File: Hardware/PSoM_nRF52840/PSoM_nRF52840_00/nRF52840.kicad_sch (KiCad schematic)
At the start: 34 parts, among them J401 Conn_01x01_Pin, J402 Conn_01x01_Pin, U401 nRF52840-QIAA-aQFN73, Y401 830108161301

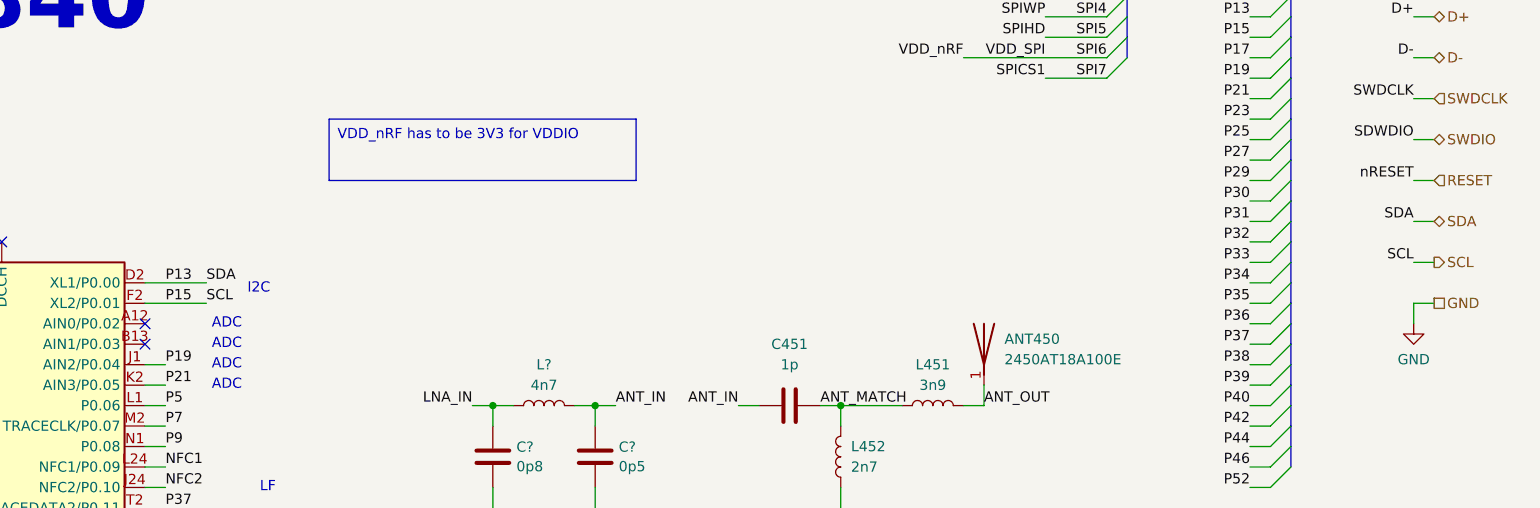
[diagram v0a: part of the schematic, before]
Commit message: moved the nrf away from the npm
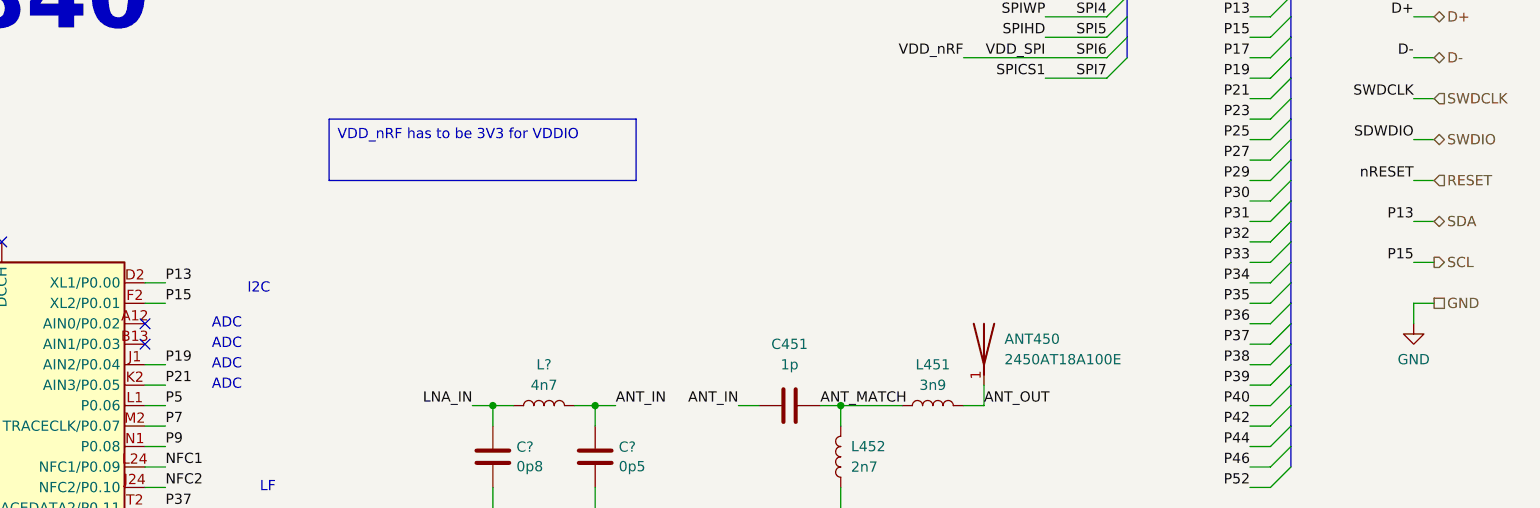
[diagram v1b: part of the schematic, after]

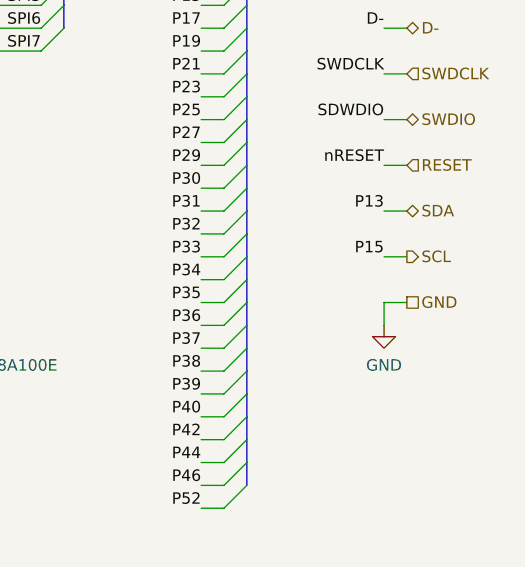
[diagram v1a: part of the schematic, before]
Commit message: moved the nrf away and re routed everything
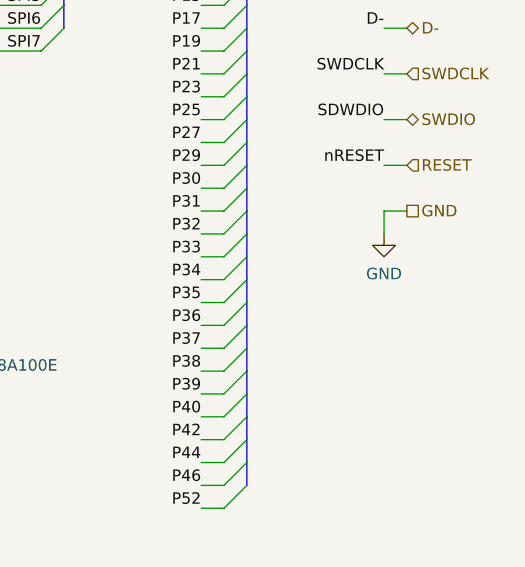
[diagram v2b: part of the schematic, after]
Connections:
- net SCL renamed P15
- net SDA renamed P13
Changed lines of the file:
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@@
 	(wire
 		(pts
-			(xy 269.24 58.42) (xy 271.78 58.42)
-		)
-		(stroke
-			(width 0)
-			(type default)
-		)
-	)
-	(wire
-		(pts
 			(xy 154.94 134.62) (xy 167.64 134.62)
 		)
@@
 	(wire
 		(pts
-			(xy 269.24 68.58) (xy 271.78 68.58)
+			(xy 269.24 58.42) (xy 271.78 58.42)
 		)
 		(stroke
@@
 	(wire
 		(pts
-			(xy 269.24 63.5) (xy 271.78 63.5)
-		)
-		(stroke
-			(width 0)
-			(type default)
-		)
-	)
-	(wire
-		(pts
 			(xy 167.64 144.78) (xy 167.64 147.32)
 		)
@@
 	(wire
 		(pts
-			(xy 269.24 71.12) (xy 269.24 68.58)
+			(xy 269.24 60.96) (xy 269.24 58.42)
 		)
 		(stroke
@@
 		)
 	)
-	(label "P15"
-		(at 269.24 63.5 180)
-		(effects
-			(font
-				(size 1.27 1.27)
-			)
-			(justify right bottom)
-		)
-	)
 	(label "SPI3"
 		(at 231.14 30.48 180)
@@
 		)
 	)
-	(label "P13"
-		(at 269.24 58.42 180)
-		(effects
-			(font
-				(size 1.27 1.27)
-			)
-			(justify right bottom)
-		)
-	)
 	(label "SPID"
 		(at 223.52 22.86 180)
@@
 		)
 	)
-	(hierarchical_label "SCL"
-		(shape output)
-		(at 271.78 63.5 0)
-		(effects
-			(font
-				(size 1.27 1.27)
-			)
-			(justify left)
-		)
-	)
-	(hierarchical_label "SDA"
-		(shape bidirectional)
-		(at 271.78 58.42 0)
-		(effects
-			(font
-				(size 1.27 1.27)
-			)
-			(justify left)
-		)
-	)
 	(hierarchical_label "RESET"
 		(shape input)
@@
 	(hierarchical_label "GND"
 		(shape passive)
-		(at 271.78 68.58 0)
+		(at 271.78 58.42 0)
 		(effects
 			(font
@@
 	(symbol
 		(lib_id "power:GND")
-		(at 269.24 71.12 0)
+		(at 269.24 60.96 0)
 		(unit 1)
 		(exclude_from_sim no)
@@
 		(fields_autoplaced yes)
 		(property "Reference" "#PWR?"
-			(at 269.24 77.47 0)
+			(at 269.24 67.31 0)
 			(effects
 				(font
@@
 		)
 		(property "Value" "GND"
-			(at 269.24 75.5634 0)
+			(at 269.24 65.4034 0)
 			(effects
 				(font
@@
 		)
 		(property "Footprint" ""
-			(at 269.24 71.12 0)
+			(at 269.24 60.96 0)
 			(effects
 				(font
@@
 		)
 		(property "Datasheet" ""
-			(at 269.24 71.12 0)
+			(at 269.24 60.96 0)
 			(effects
 				(font
@@
 		)
 		(property "Description" ""
-			(at 269.24 71.12 0)
+			(at 269.24 60.96 0)
 			(effects
 				(font

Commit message: TODO: RF and GND vias
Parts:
- removed D?: LED, LED_SMD:LED_0402_1005Metric, symbol Component lib:LED
- removed R?: 2k, Resistor_SMD:R_0402_1005Metric, symbol Component lib:R

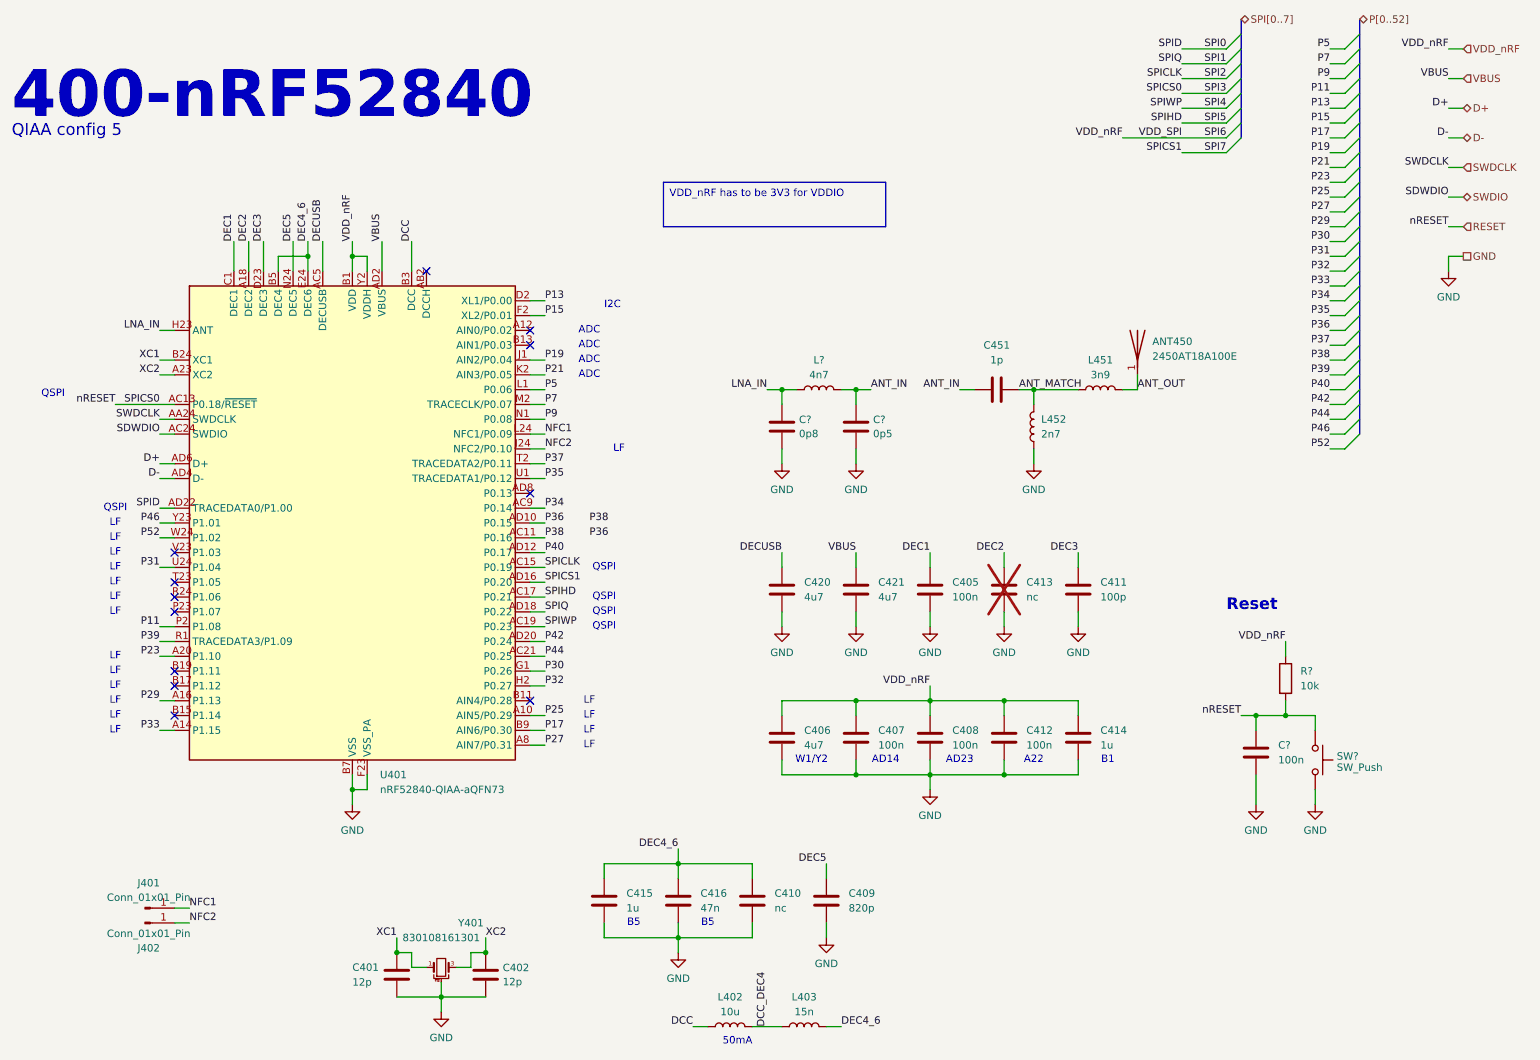
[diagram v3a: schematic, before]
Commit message: added ufl connector and trace width for 50ohm rf
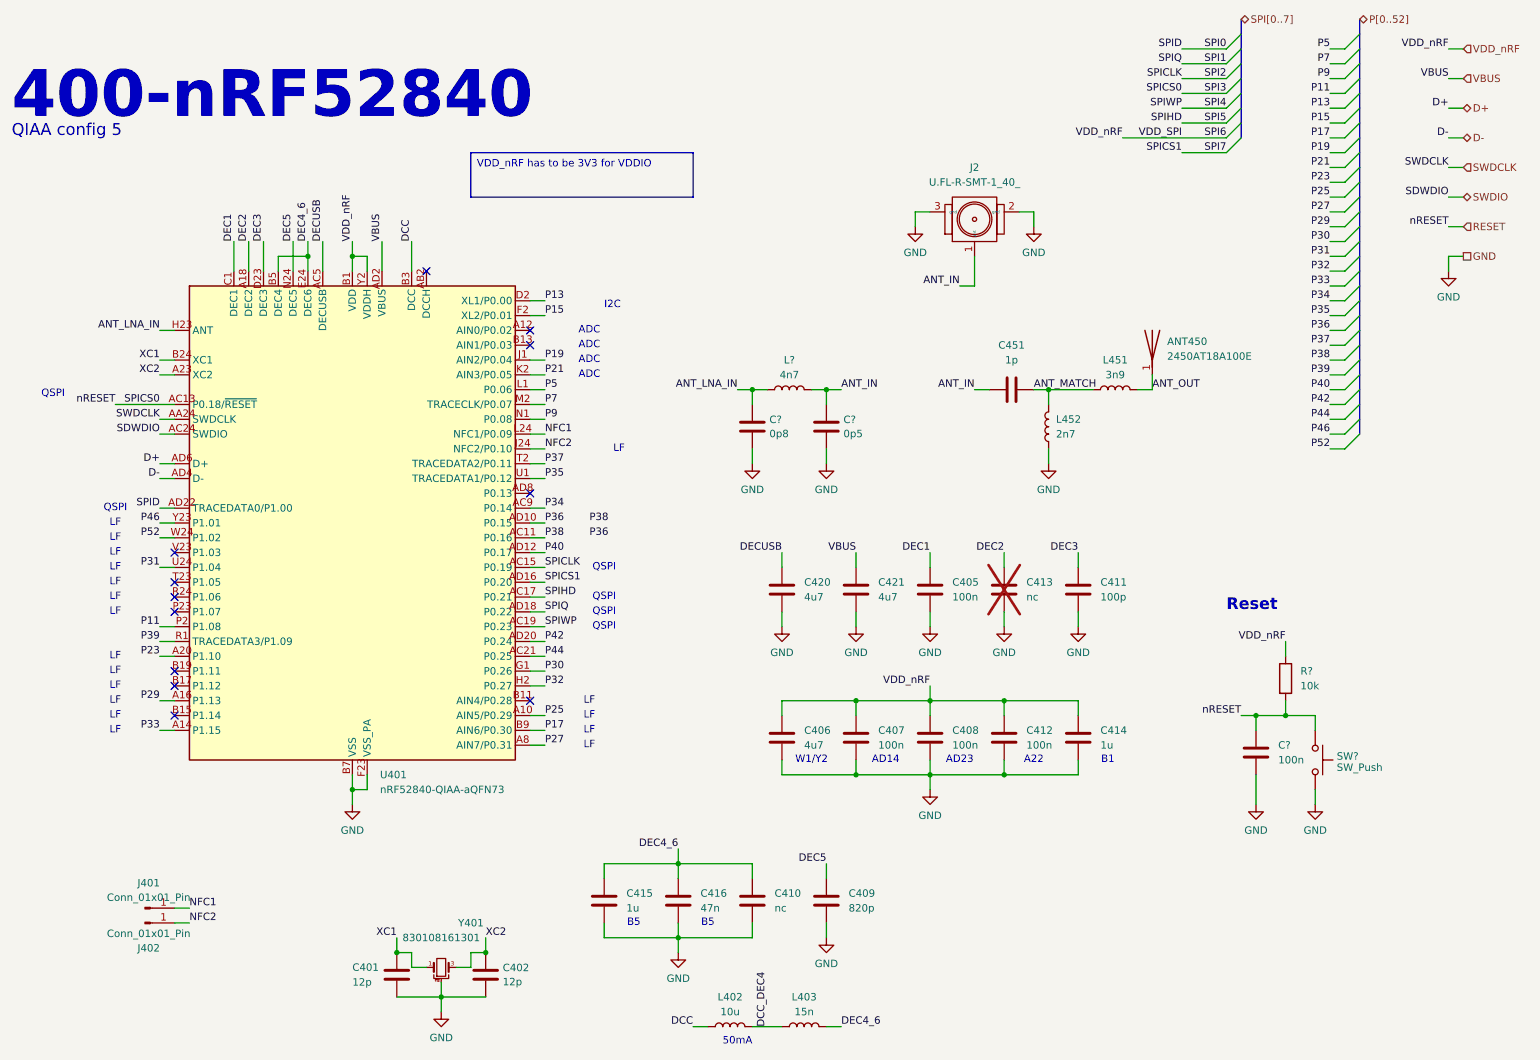
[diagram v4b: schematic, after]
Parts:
- added J2: U.FL-R-SMT-1_40_, Component_lib:u.fl, symbol Component_lib:U.FL-R-SMT-1_40_
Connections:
- net ANT_IN: now also J2.1 (ant)
- net GND: now also J2.2 (gnd), J2.3 (gnd)
- net LNA_IN renamed ANT_LNA_IN
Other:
- moved on the sheet: ANT450, C451, C?, L451, L452, L?

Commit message: finished routing + generated gerbers
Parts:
- removed ANT450: 2450AT18A100E, Component_lib:ANTC3216X140N, symbol Component_lib:2450AT18A100E
- removed C451: 1p, Capacitor_SMD:C_0201_0603Metric, symbol Component lib:C
- removed L451: 3n9, Inductor_SMD:L_0201_0603Metric, symbol Component lib:L
- removed L452: 2n7, Inductor_SMD:L_0201_0603Metric, symbol Component lib:L
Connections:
- net GND: no longer J2.3 (gnd)
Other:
- moved on the sheet: C?, J2, L?
